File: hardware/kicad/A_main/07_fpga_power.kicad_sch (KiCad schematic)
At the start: 0 parts

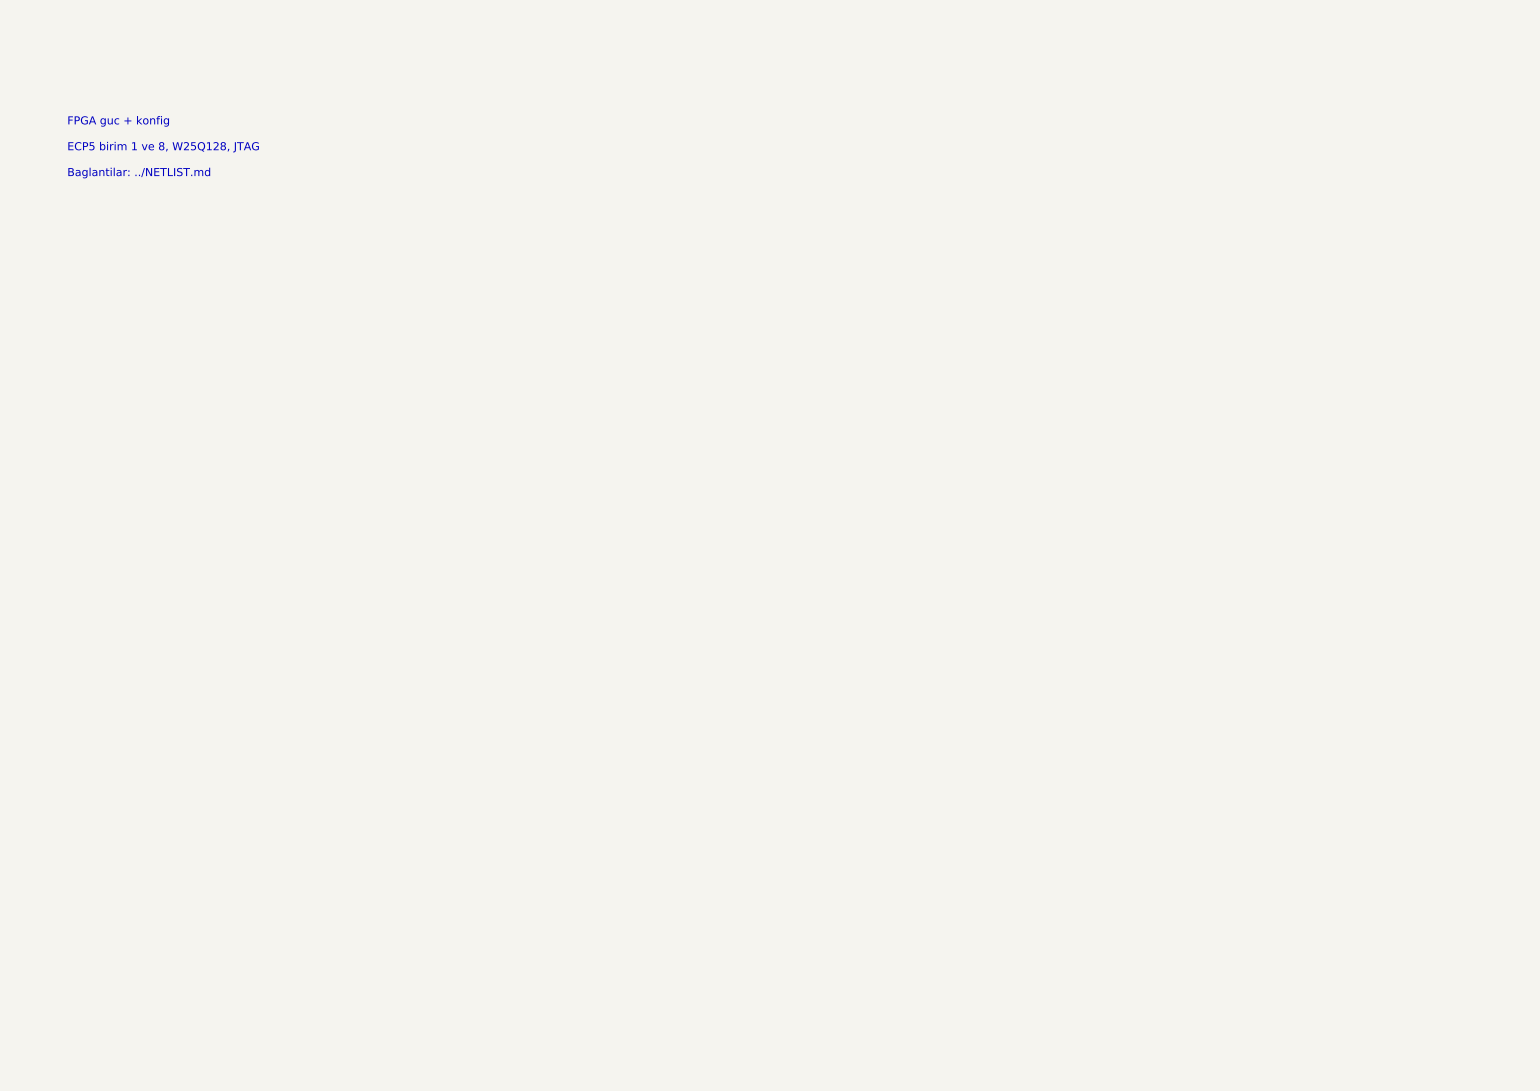
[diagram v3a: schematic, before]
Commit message: Correct the schematic faults that ERC cannot find
An agent examined the three schematics against the datasheets. ERC
reported zero violations before and after this work. None of these
faults are visible to ERC.

The comparator for the external 10 MHz reference was in shutdown. The
SHDN pin of the TLV3501 went to +3V3. Sixteen DRV8833 devices had VCP
and VINT unconnected. Without the charge pump none of the 28 filter
relays can latch. Seven regulators had no decoupling capacitor within
18 mm to 94 mm. On board D the nearest +12V capacitor to an LM358 was
227 mm away on a 275 mm board.

The PE4312 devices had no series 10k resistor on pin 3. The datasheet
makes this necessary for the attenuation accuracy. Their exposed pad
was 2.6 mm against 2.15 mm. The BOM did not give the load capacitance
of the crystal. This work added 60 parts and changed 4 footprints.

The worst fault was in the tool chain. lib/gen_symbols.py still made
the old pin numbers. The five corrections went into the symbol
library by hand and not into its generator. A new library would have
removed all of them.

The thermal vias are now a decision from the measured clearance and
the dissipation. This work removed them from the PE4312, the RTL8211F
and the ADCLK846. They stay on the DRV8833 and on the LM5164, which
is a 1 W buck converter.

Two checks are new. sema_denetim compares the pin names with the
nets. netlist_denetim locks 22 pin-to-net expectations from the
datasheets and does not need a board.

The boards were built again with these corrections. The chain now
adds the test points: 10 on board A, 7 on board C and 15 on board D.
Each board has 3 fiducials. Every pad has a net.
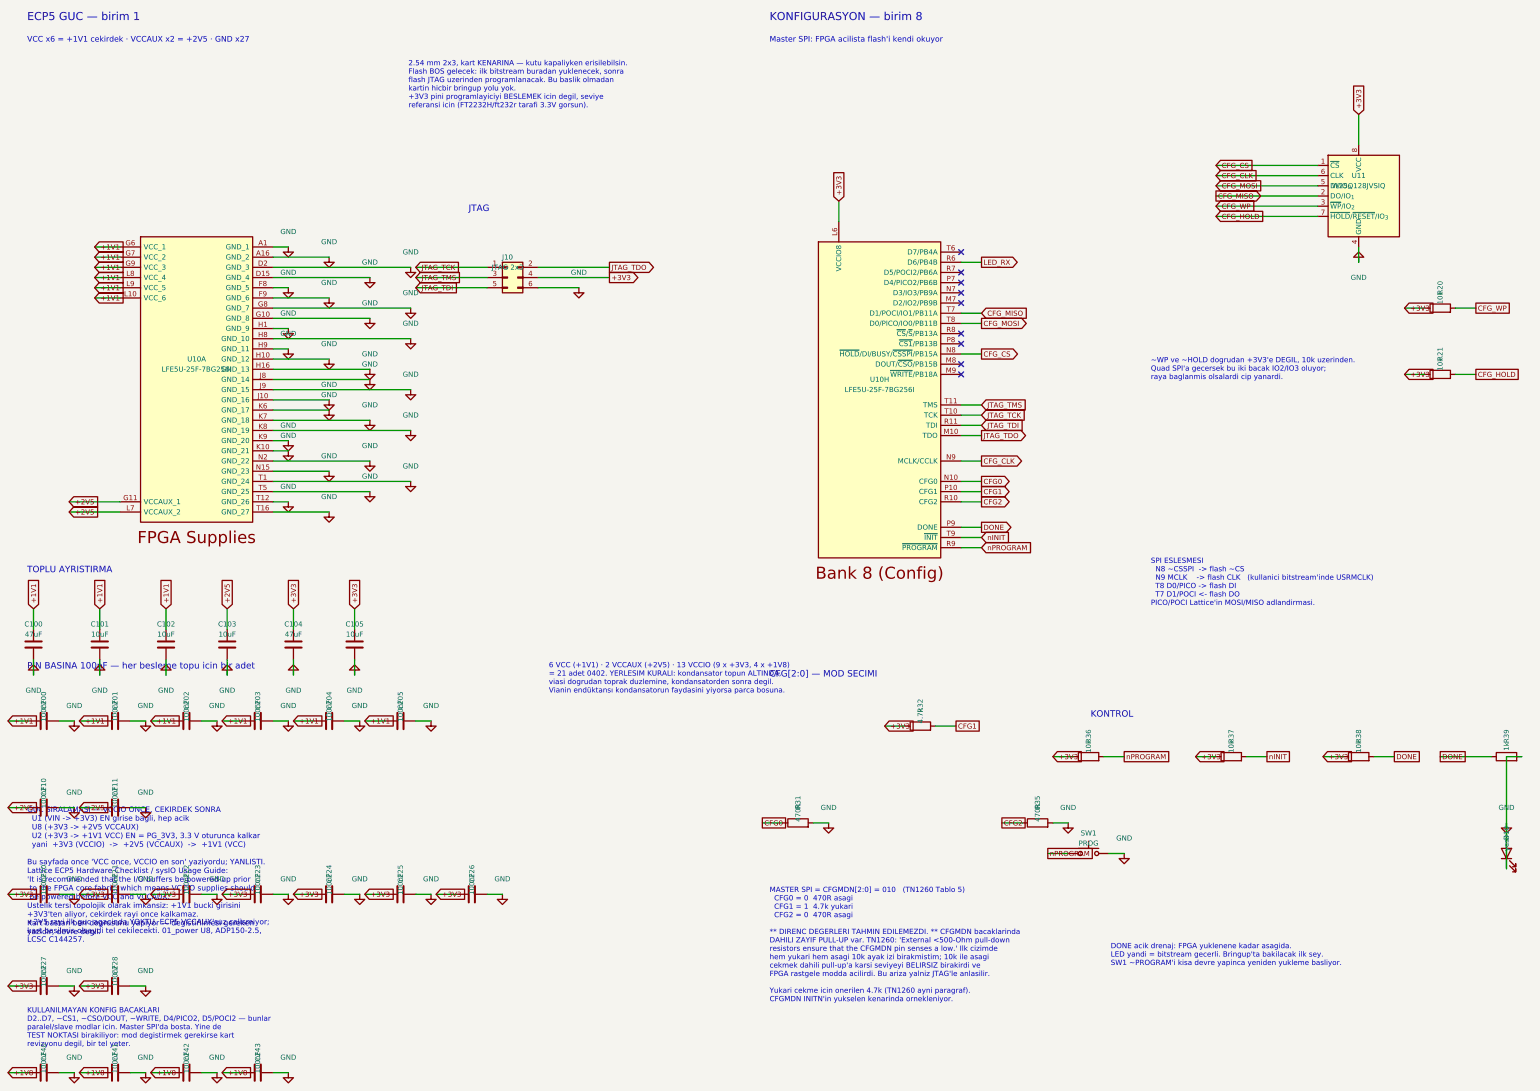
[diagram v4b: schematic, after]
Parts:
- added C100, C104: 47uF, Capacitor_SMD:C_1206_3216Metric, symbol Device:C
- added C101, C102, C103, C105: 10uF, Capacitor_SMD:C_0603_1608Metric, symbol Device:C
- added C200, C201, C202, C203, C204, C205, C210, C211, C220, C221, C222, C223, C224, C225, C226, C227, C228, C240, C241, C242, C243: 100nF, Capacitor_SMD:C_0402_1005Metric, symbol Device:C
- added D10: yesil, LED_SMD:LED_0603_1608Metric, symbol Device:LED
- added J10: JTAG 2x3, Connector_PinHeader_2.54mm:PinHeader_2x03_P2.54mm_Vertical, symbol Connector_Generic:Conn_02x03_Odd_Even
- added R20, R21, R36, R37, R38: 10k, Resistor_SMD:R_0603_1608Metric, symbol Device:R
- added R31, R35: 470R, Resistor_SMD:R_0603_1608Metric, symbol Device:R
- added R32: 4.7k, Resistor_SMD:R_0603_1608Metric, symbol Device:R
- added R39: 1k, Resistor_SMD:R_0603_1608Metric, symbol Device:R
- added SW1: PROG, Button_Switch_SMD:SW_SPST_TL3342, symbol Switch:SW_Push
- added U10: LFE5U-25F-7BG256I, Package_BGA:BGA-256_14.0x14.0mm_Layout16x16_P0.8mm_Ball0.45mm_Pad0.32mm_NSMD, symbol dogrudan-sdr:ECP5-BGA256
- added U11: W25Q128JVSIQ, Package_SO:SOIC-8_5.3x5.3mm_P1.27mm, symbol Memory_Flash:W25Q128JVS
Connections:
- new net +1V1: C100.1, C101.1, C102.1, C200.1, C201.1, C202.1, C203.1, C204.1, C205.1, U10.G6 (VCC_1), U10.G7 (VCC_2), U10.G9 (VCC_3), U10.L10 (VCC_6), U10.L8 (VCC_4), U10.L9 (VCC_5)
- new net +1V8: C240.1, C241.1, C242.1, C243.1
- new net +2V5: C103.1, C210.1, C211.1, U10.G11 (VCCAUX_1), U10.L7 (VCCAUX_2)
- new net +3V3: C104.1, C105.1, C220.1, C221.1, C222.1, C223.1, C224.1, C225.1, C226.1, C227.1, C228.1, J10.4 (Pin_4), R20.1, R21.1, R32.1, R36.1, R37.1, R38.1, U10.L6 (VCCIO8), U11.8 (VCC)
- new net CFG0: R31.1, U10.N10 (CFG0)
- new net CFG1: R32.2, U10.P10 (CFG1)
- new net CFG2: R35.1, U10.R10 (CFG2)
- new net CFG_CLK: U10.N9 (MCLK/CCLK), U11.6 (CLK)
- new net CFG_CS: U10.N8 (~{HOLD}/DI/BUSY/~{CSSPI}/PB15A), U11.1 (~{CS})
- new net CFG_HOLD: R21.2, U11.7 (~{HOLD}/~{RESET}/IO_{3})
- new net CFG_MISO: U10.T7 (D1/POCI/IO1/PB11A), U11.2 (DO/IO_{1})
- new net CFG_MOSI: U10.T8 (D0/PICO/IO0/PB11B), U11.5 (DI/IO_{0})
- new net CFG_WP: R20.2, U11.3 (~{WP}/IO_{2})
- new net DONE: R38.2, R39.1, U10.P9 (DONE)
- new net GND: C100.2, C101.2, C102.2, C103.2, C104.2, C105.2, C200.2, C201.2, C202.2, C203.2, C204.2, C205.2, C210.2, C211.2, C220.2, C221.2, C222.2, C223.2, C224.2, C225.2, C226.2, C227.2, C228.2, C240.2, C241.2, C242.2, C243.2, D10.1 (K), D10.2 (A), J10.6 (Pin_6), R31.2, R35.2, R39.2, SW1.2, U10.A1 (GND_1), U10.A16 (GND_2), U10.D15 (GND_4), U10.D2 (GND_3), U10.F8 (GND_5), U10.F9 (GND_6), U10.G10 (GND_8), U10.G8 (GND_7), U10.H1 (GND_9), U10.H10 (GND_12), U10.H16 (GND_13), U10.H8 (GND_10), U10.H9 (GND_11), U10.J10 (GND_16), U10.J8 (GND_14), U10.J9 (GND_15), U10.K10 (GND_21), U10.K6 (GND_17), U10.K7 (GND_18), U10.K8 (GND_19), U10.K9 (GND_20), U10.N15 (GND_23), U10.N2 (GND_22), U10.T1 (GND_24), U10.T12 (GND_26), U10.T16 (GND_27), U10.T5 (GND_25), U11.4 (GND)
- new net JTAG_TCK: J10.1 (Pin_1), U10.T10 (TCK)
- new net JTAG_TDI: J10.5 (Pin_5), U10.R11 (TDI)
- new net JTAG_TDO: J10.2 (Pin_2), U10.M10 (TDO)
- new net JTAG_TMS: J10.3 (Pin_3), U10.T11 (TMS)
- new net LED_RX: U10.R6 (D6/PB4B)
- new net nINIT: R37.2, U10.T9 (~{INIT})
- new net nPROGRAM: R36.2, SW1.1, U10.R9 (~{PROGRAM})
- no-connect marks 0 -> 9
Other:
- note added: "+2V5 rayi ilk guc agacinda YOKTU. ECP5 VCCAUX'suz calismiyor; kart basilmis olsaydi tel cekilecekti. 01_power U8, ADP150-2.5, LCSC C144257."
- note added: "2.54 mm 2x3, kart KENARINA — kutu kapaliyken erisilebilsin. Flash BOS gelecek: ilk bitstream buradan yuklenecek, sonra flash JTAG uzerinden programlanacak. Bu baslik olmadan kartin hicbir bringup yolu yok. +3V3 pini programlayiciyi BESLEMEK icin degil, seviye referansi icin (FT2232H/ft232r tarafi 3.3V gorsun)."
- note added: "6 VCC (+1V1) · 2 VCCAUX (+2V5) · 13 VCCIO (9 x +3V3, 4 x +1V8) = 21 adet 0402. YERLESIM KURALI: kondansator topun ALTINDA, viasi dogrudan toprak duzlemine, kondansatorden sonra degil. Vianin endüktansı kondansatorun faydasini yiyorsa parca bosuna."
- note added: "CFG[2:0] — MOD SECIMI"
- note added: "DONE acik drenaj: FPGA yuklenene kadar asagida. LED yandi = bitstream gecerli. Bringup'ta bakilacak ilk sey. SW1 ~PROGRAM'i kisa devre yapinca yeniden yukleme basliyor."
- note added: "ECP5 GUC — birim 1"
- note added: "GUC SIRALAMASI — VCCIO ONCE, CEKIRDEK SONRA U1 (VIN -> +3V3) EN girise bagli, hep acik U8 (+3V3 -> +2V5 VCCAUX) U2 (+3V3 -> +1V1 VCC) EN = PG_3V3, 3.3 V oturunca kalkar yani +3V3 (VCCIO) -> +2V5 (VCCAUX) -> +1V1 (VCC) Bu sayfada once 'VCC once, VCCIO en son' yaziyordu; YANLISTI. Lattice ECP5 Hardware Checklist / sysIO Usage Guide: 'It is recommended that the I/O buffers be powered-up prior to the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"
- note added: "JTAG"
- note added: "KONFIGURASYON — birim 8"
- note added: "KONTROL"
- note added: "KULLANILMAYAN KONFIG BACAKLARI D2..D7, ~CS1, ~CSO/DOUT, ~WRITE, D4/PICO2, D5/POCI2 — bunlar paralel/slave modlar icin. Master SPI'da bosta. Yine de TEST NOKTASI birakiliyor: mod degistirmek gerekirse kart revizyonu degil, bir tel yeter."
- note added: "MASTER SPI = CFGMDN[2:0] = 010 (TN1260 Tablo 5) CFG0 = 0 470R asagi CFG1 = 1 4.7k yukari CFG2 = 0 470R asagi ** DIRENC DEGERLERI TAHMIN EDILEMEZDI. ** CFGMDN bacaklarinda DAHILI ZAYIF PULL-UP var. TN1260: 'External <500-Ohm pull-down resistors ensure that the CFGMDN pin senses a low.' Ilk cizimde hem yukari hem asagi 10k ayak izi birakmistim; 10k ile asagi cekmek dahili pull-up'a karsi seviyeyi B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"
- note added: "Master SPI: FPGA acilista flash'i kendi okuyor"
- note added: "PIN BASINA 100nF — her besleme topu icin bir adet"
- note added: "SPI ESLESMESI N8 ~CSSPI -> flash ~CS N9 MCLK -> flash CLK (kullanici bitstream'inde USRMCLK) T8 D0/PICO -> flash DI T7 D1/POCI <- flash DO PICO/POCI Lattice'in MOSI/MISO adlandirmasi."
- note added: "TOPLU AYRISTIRMA"
- note added: "VCC x6 = +1V1 cekirdek · VCCAUX x2 = +2V5 · GND x27"
- note added: "~WP ve ~HOLD dogrudan +3V3'e DEGIL, 10k uzerinden. Quad SPI'a gecersek bu iki bacak IO2/IO3 oluyor; raya baglanmis olsalardi cip yanardi."
- note removed: "FPGA guc + konfig ECP5 birim 1 ve 8, W25Q128, JTAG Baglantilar: ../NETLIST.md"
- title: FPGA guc + konfig -> FPGA guc + konfigurasyon
